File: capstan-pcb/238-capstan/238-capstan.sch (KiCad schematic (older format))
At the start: 53 parts, among them CN1 CN1, IC1 BA6303F, IC2 4013, IC3 BA6411, J1 0, J2 0

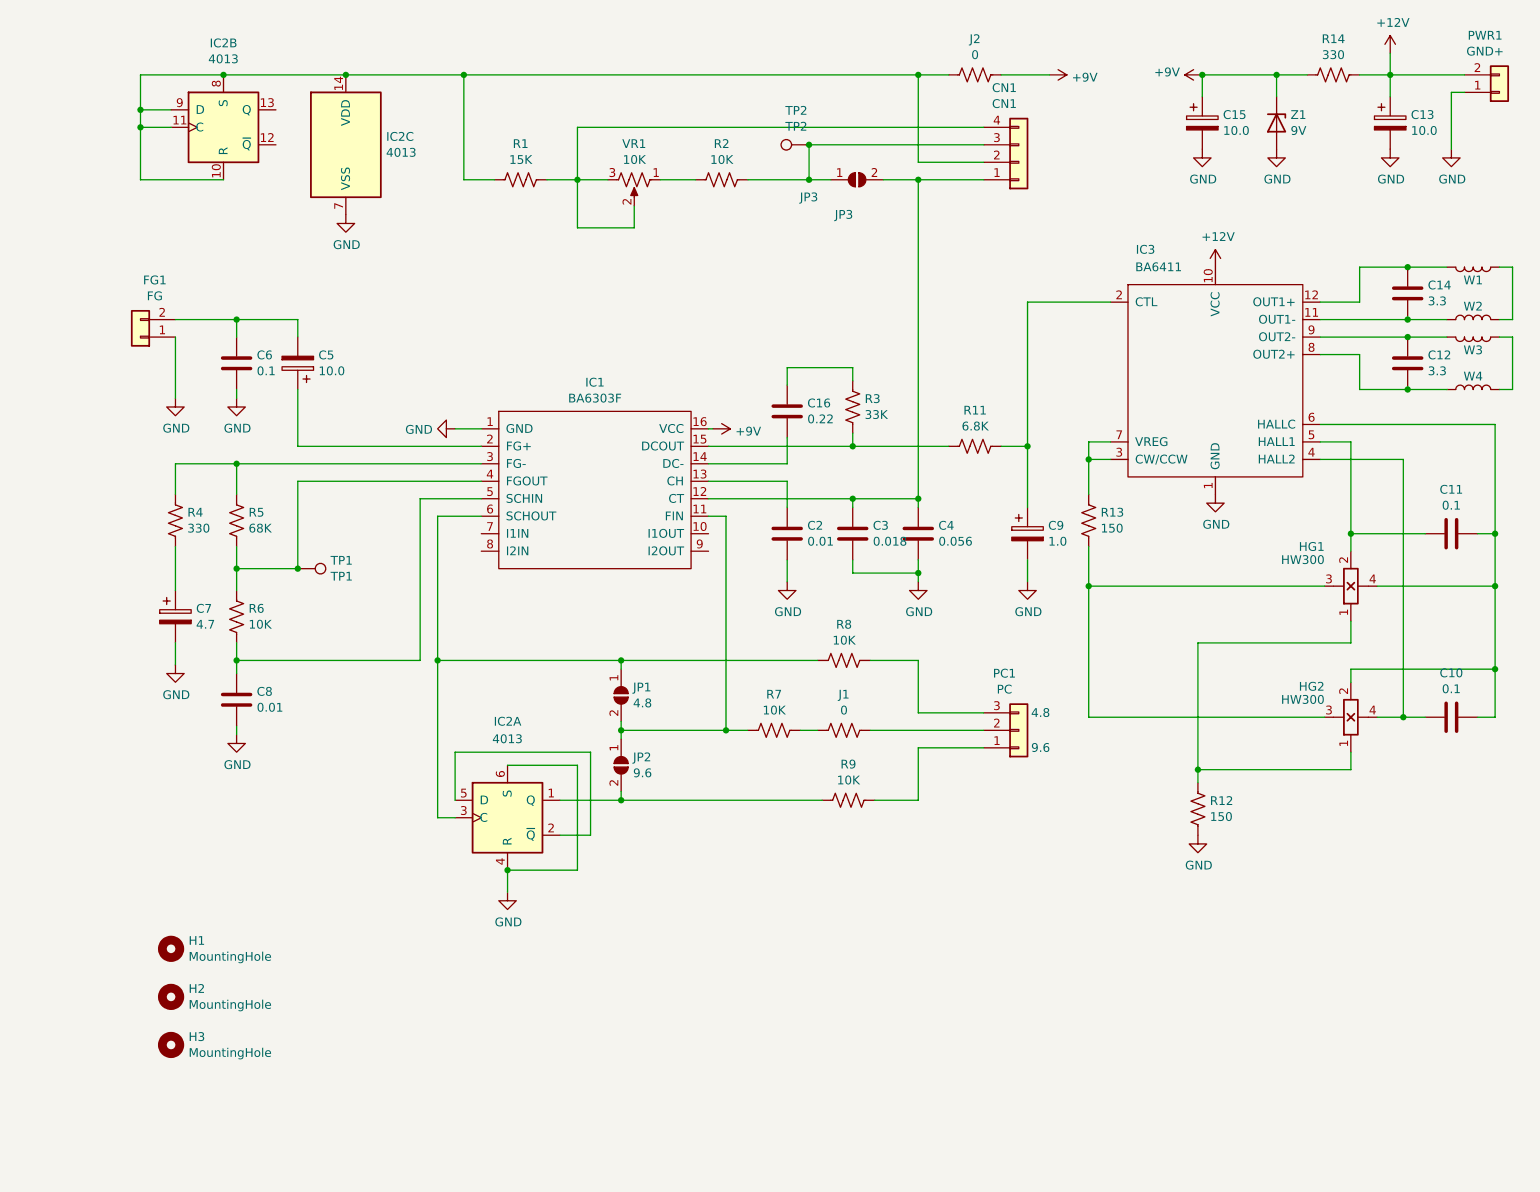
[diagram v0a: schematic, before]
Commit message: Capstan PCB v2024-09-11, clarified schematic
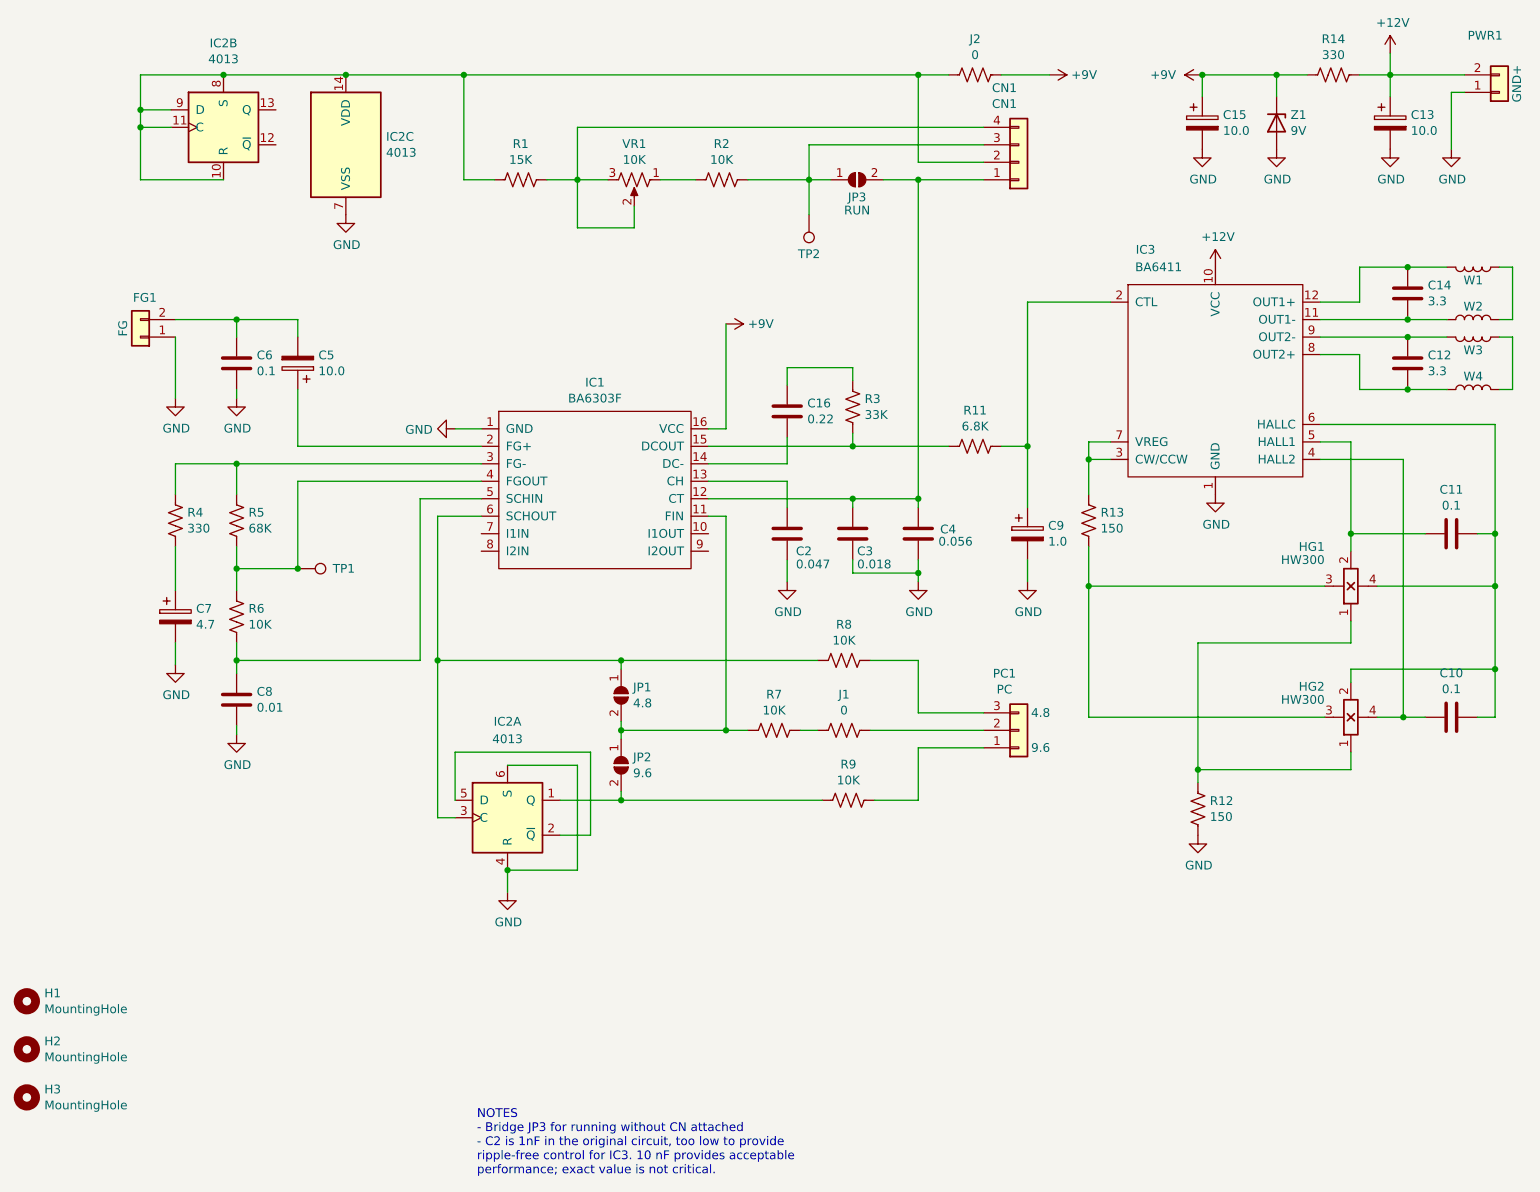
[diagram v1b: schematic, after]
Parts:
- C2: value 0.01 -> 0.047
- IC1: footprint Package_SO:SO-16_5.3x10.2mm_P1.27mm -> Package_SO:SOIC-16_4.55x10.3mm_P1.27mm
- JP3: value JP3 -> RUN
- TP1: footprint TestPoint:TestPoint_Pad_D2.5mm -> TestPoint:TestPoint_Pad_D1.5mm
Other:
- note added: "NOTES\n- Bridge JP3 for running without CN attached\n- C2 is 1nF in the original circuit, too low to provide\nripple-free control for IC3. 10 nF provides acceptable\nperformance; exact value is not critical."
- moved on the sheet: H1, H2, H3, TP2
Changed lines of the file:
@@
 Sheet 1 1
 Title "Tascam 238 Capstan Motor"
-Date "2024-08-15"
-Rev "2"
+Date "2024-09-12"
+Rev "3"
 Comp "238pro.com"
 Comment1 ""
@@
 F 0 "IC1" H 4325 4490 50  0000 C CNN
 F 1 "BA6303F" H 4325 4399 50  0000 C CNN
-F 2 "Package_SO:SO-16_5.3x10.2mm_P1.27mm" H 4325 3325 50  0001 C CNN
+F 2 "Package_SO:SOIC-16_4.55x10.3mm_P1.27mm" H 4325 3325 50  0001 C CNN
 F 3 "" H 3775 3425 50  0001 C CNN
 	1    4325 3875
@@
 U 1 1 66AE4D87
 P 5800 4125
-F 0 "C3" H 5685 4079 50  0000 R CNN
-F 1 "0.018" H 5685 4170 50  0000 R CNN
+F 0 "C3" H 5775 4225 50  0000 R CNN
+F 1 "0.018" H 5775 4300 50  0000 R CNN
 F 2 "denis:238_C3" H 5838 3975 50  0001 C CNN
 F 3 "~" H 5800 4125 50  0001 C CNN
@@
 U 1 1 66AE5535
 P 6175 4125
-F 0 "C4" H 6290 4171 50  0000 L CNN
+F 0 "C4" H 6300 4150 50  0000 L CNN
 F 1 "0.056" H 6290 4080 50  0000 L CNN
 F 2 "denis:238_C4" H 6213 3975 50  0001 C CNN
@@
 U 1 1 66AE5D8E
 P 5425 4125
-F 0 "C2" H 5540 4171 50  0000 L CNN
-F 1 "0.01" H 5540 4080 50  0000 L CNN
+F 0 "C2" H 5475 4025 50  0000 L CNN
+F 1 "0.047" H 5475 3950 50  0000 L CNN
 F 2 "Capacitor_SMD:C_1206_3216Metric_Pad1.33x1.80mm_HandSolder" H 5463 3975 50  0001 C CNN
 F 3 "~" H 5425 4125 50  0001 C CNN
@@
 U 1 1 66AE9878
 P 2625 4325
-F 0 "TP1" V 2579 4513 50  0000 L CNN
-F 1 "TP1" V 2670 4513 50  0000 L CNN
-F 2 "TestPoint:TestPoint_Pad_D2.5mm" H 2825 4325 50  0001 C CNN
+F 0 "TP1" V 2625 4525 50  0000 L CNN
+F 1 "TP1" V 2670 4513 50  0001 L CNN
+F 2 "TestPoint:TestPoint_Pad_D1.5mm" H 2825 4325 50  0001 C CNN
 F 3 "~" H 2825 4325 50  0001 C CNN
 	1    2625 4325
@@
 L Connector:TestPoint TP2
 U 1 1 66AEA42E
-P 5550 1900
-F 0 "TP2" V 5745 1972 50  0000 C CNN
-F 1 "TP2" V 5654 1972 50  0000 C CNN
-F 2 "TestPoint:TestPoint_Pad_D2.5mm" H 5750 1900 50  0001 C CNN
-F 3 "~" H 5750 1900 50  0001 C CNN
-	1    5550 1900
-	0    -1   -1   0
+P 5550 2300
+F 0 "TP2" H 5550 2525 50  0000 C CNN
+F 1 "TP2" H 5550 2525 50  0001 C CNN
+F 2 "TestPoint:TestPoint_Pad_D2.5mm" H 5750 2300 50  0001 C CNN
+F 3 "~" H 5750 2300 50  0001 C CNN
+	1    5550 2300
+	-1   0    0    1
 $EndComp
 $Comp
@@
 U 1 1 66AEC480
 P 1725 3000
-F 0 "FG1" H 1643 2675 50  0000 C CNN
-F 1 "FG" H 1643 2766 50  0000 C CNN
+F 0 "FG1" H 1700 2775 50  0000 C CNN
+F 1 "FG" V 1825 2950 50  0000 C CNN
 F 2 "denis:238_2_wire_conn" H 1725 3000 50  0001 C CNN
 F 3 "~" H 1725 3000 50  0001 C CNN
@@
 P 9500 1600
 F 0 "PWR1" H 9418 1275 50  0000 C CNN
-F 1 "GND+" H 9418 1366 50  0000 C CNN
+F 1 "GND+" V 9600 1550 50  0000 C CNN
 F 2 "denis:238_2_wire_conn" H 9500 1600 50  0001 C CNN
 F 3 "~" H 9500 1600 50  0001 C CNN
@@
 U 1 1 66AF5822
 P 5825 2100
-F 0 "JP3" H 5750 1900 50  0000 C CNN
-F 1 "JP3" H 5550 2000 50  0000 C CNN
+F 0 "JP3" H 5825 2000 50  0000 C CNN
+F 1 "RUN" H 5825 1925 50  0000 C CNN
 F 2 "Jumper:SolderJumper-2_P1.3mm_Open_RoundedPad1.0x1.5mm" H 5825 2100 50  0001 C CNN
 F 3 "~" H 5825 2100 50  0001 C CNN
@@
 Wire Wire Line
 	5425 3175 5425 3275
-Wire Wire Line
-	4975 3525 5000 3525
 $Comp
 L power:+9V #PWR0109
 U 1 1 66CEAE92
-P 5000 3525
-F 0 "#PWR0109" H 5000 3375 50  0001 C CNN
-F 1 "+9V" V 5015 3653 50  0000 L CNN
-F 2 "" H 5000 3525 50  0001 C CNN
-F 3 "" H 5000 3525 50  0001 C CNN
-	1    5000 3525
+P 5075 2925
+F 0 "#PWR0109" H 5075 2775 50  0001 C CNN
+F 1 "+9V" V 5075 3050 50  0000 L CNN
+F 2 "" H 5075 2925 50  0001 C CNN
+F 3 "" H 5075 2925 50  0001 C CNN
+	1    5075 2925
 	0    1    1    0
 $EndComp
@@
 P 6925 1500
 F 0 "#PWR0111" H 6925 1350 50  0001 C CNN
-F 1 "+9V" V 6940 1628 50  0000 L CNN
+F 1 "+9V" V 6925 1625 50  0000 L CNN
 F 2 "" H 6925 1500 50  0001 C CNN
 F 3 "" H 6925 1500 50  0001 C CNN
@@
 P 7800 1500
 F 0 "#PWR0121" H 7800 1350 50  0001 C CNN
-F 1 "+9V" V 7815 1628 50  0000 L CNN
+F 1 "+9V" V 7800 1650 50  0000 L CNN
 F 2 "" H 7800 1500 50  0001 C CNN
 F 3 "" H 7800 1500 50  0001 C CNN
@@
 	5975 2100 6175 2100
 Connection ~ 6175 2100
-Connection ~ 5550 1900
 Wire Wire Line
 	5075 4025 5075 5250
@@
 L Mechanical:MountingHole H3
 U 1 1 67A9CC42
-P 1900 7050
-F 0 "H3" H 2000 7096 50  0000 L CNN
-F 1 "MountingHole" H 2000 7005 50  0000 L CNN
-F 2 "MountingHole:MountingHole_2.1mm" H 1900 7050 50  0001 C CNN
-F 3 "~" H 1900 7050 50  0001 C CNN
-	1    1900 7050
+P 1075 7350
+F 0 "H3" H 1175 7396 50  0000 L CNN
+F 1 "MountingHole" H 1175 7305 50  0000 L CNN
+F 2 "MountingHole:MountingHole_2.1mm" H 1075 7350 50  0001 C CNN
+F 3 "~" H 1075 7350 50  0001 C CNN
+	1    1075 7350
 	1    0    0    -1
 $EndComp
@@
 L Mechanical:MountingHole H2
 U 1 1 67A9E9DA
-P 1900 6775
-F 0 "H2" H 2000 6821 50  0000 L CNN
-F 1 "MountingHole" H 2000 6730 50  0000 L CNN
-F 2 "MountingHole:MountingHole_2.1mm" H 1900 6775 50  0001 C CNN
-F 3 "~" H 1900 6775 50  0001 C CNN
-	1    1900 6775
+P 1075 7075
+F 0 "H2" H 1175 7121 50  0000 L CNN
+F 1 "MountingHole" H 1175 7030 50  0000 L CNN
+F 2 "MountingHole:MountingHole_2.1mm" H 1075 7075 50  0001 C CNN
+F 3 "~" H 1075 7075 50  0001 C CNN
+	1    1075 7075
 	1    0    0    -1
 $EndComp
@@
 L Mechanical:MountingHole H1
 U 1 1 67A9F7A2
-P 1900 6500
-F 0 "H1" H 2000 6546 50  0000 L CNN
-F 1 "MountingHole" H 2000 6455 50  0000 L CNN
-F 2 "MountingHole:MountingHole_2.1mm" H 1900 6500 50  0001 C CNN
-F 3 "~" H 1900 6500 50  0001 C CNN
-	1    1900 6500
+P 1075 6800
+F 0 "H1" H 1175 6846 50  0000 L CNN
+F 1 "MountingHole" H 1175 6755 50  0000 L CNN
+F 2 "MountingHole:MountingHole_2.1mm" H 1075 6800 50  0001 C CNN
+F 3 "~" H 1075 6800 50  0001 C CNN
+	1    1075 6800
 	1    0    0    -1
 $EndComp
@@
 	0    -1   -1   0
 $EndComp
+Wire Wire Line
+	5550 2100 5550 2300
+Wire Wire Line
+	5075 2925 5075 3525
+Wire Wire Line
+	5075 3525 4975 3525
+Text Notes 3650 7800 0    50   ~ 0
+NOTES\n- Bridge JP3 for running without CN attached\n- C2 is 1nF in the original circuit, too low to provide\nripple-free control for IC3. 10 nF provides acceptable\nperformance; exact value is not critical.
 $EndSCHEMATC
